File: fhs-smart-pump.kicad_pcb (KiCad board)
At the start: 2 copper layers, 92 x 87 mm, 30 parts, among them J1 Screw_Terminal_01x09, J2 Conn_01x02, J3 Screw_Terminal_01x02, K1 G5NB, K2 G5NB, Q1 2SA1015, Q2 2SA1015, U1 LM2596T-5, U2 PC817, U3 ESP32-C3_SUPERMINI_TH, U4 PC817

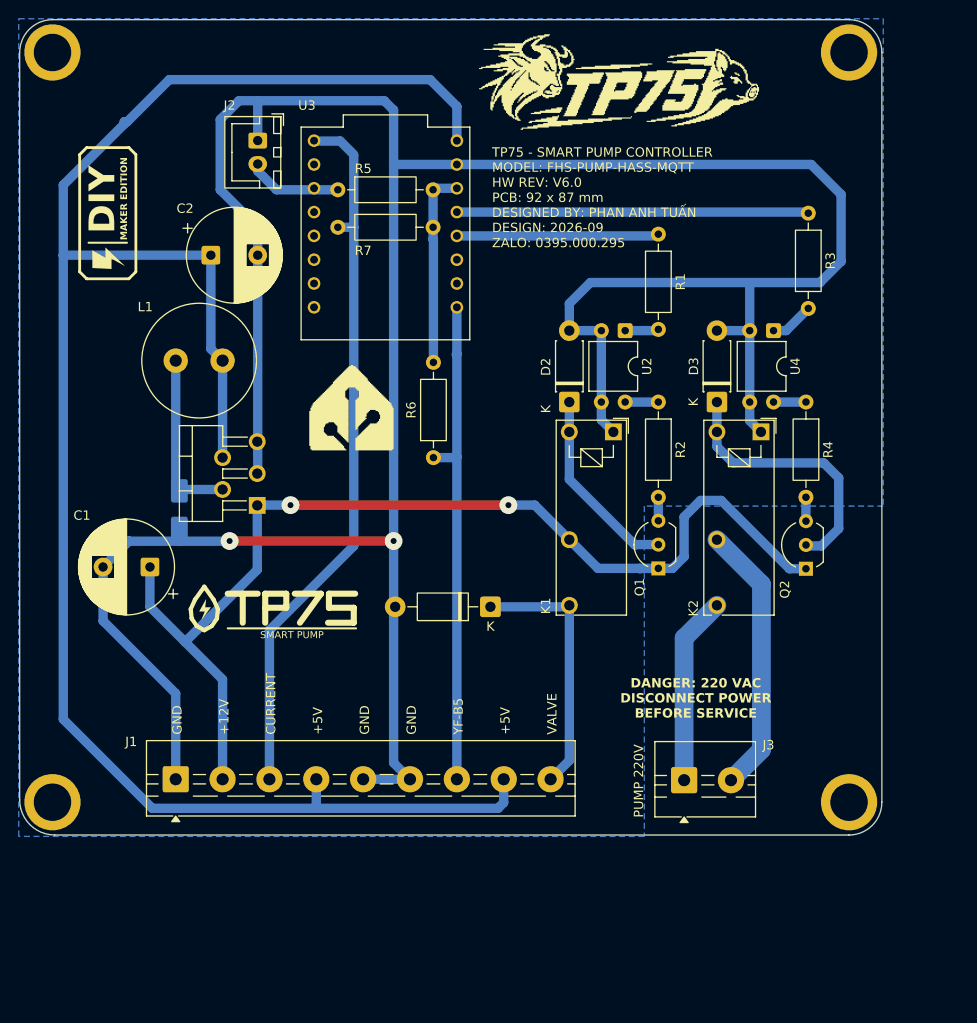
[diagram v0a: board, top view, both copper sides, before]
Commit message: đổi chân nguồn sang 5.5
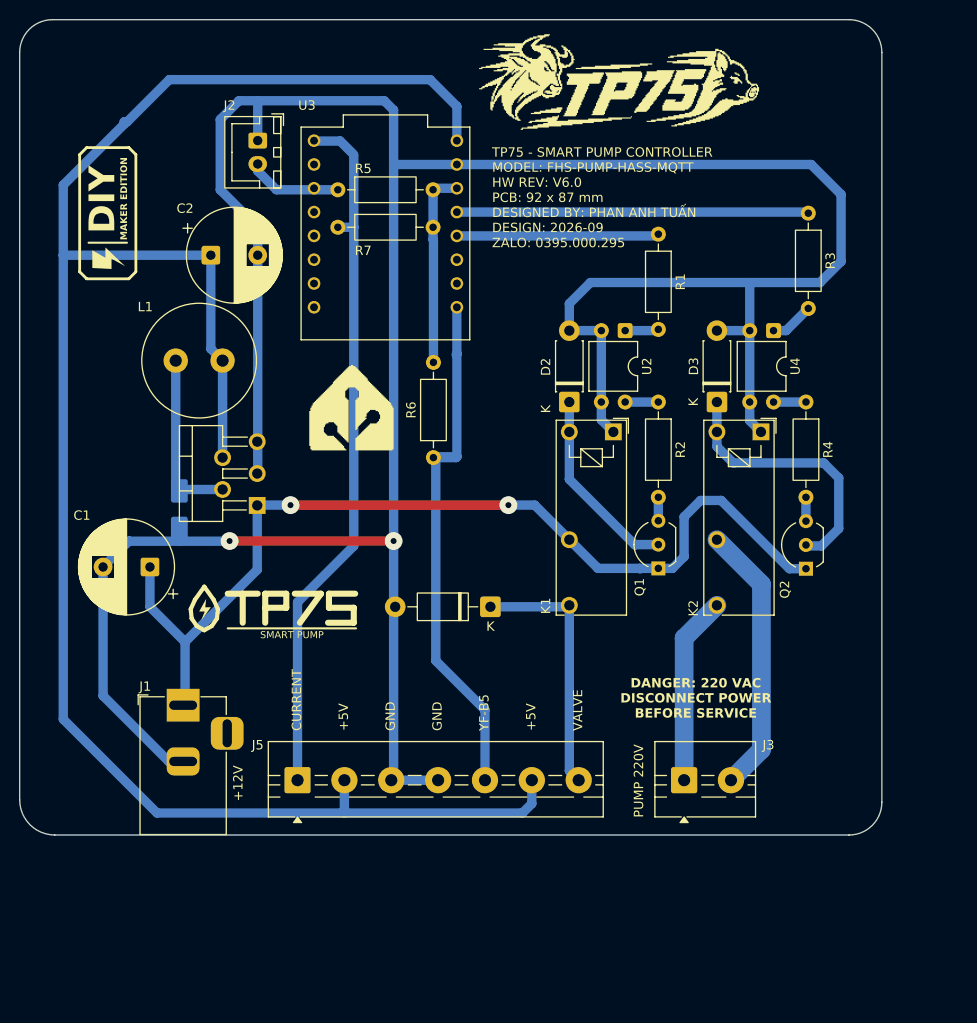
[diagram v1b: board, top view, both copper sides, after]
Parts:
- removed MECH1: LK-PLC02_92x87, 
- added J5: Screw_Terminal_01x07, TerminalBlock:TerminalBlock_MaiXu_MX126-5.0-07P_1x07_P5.00mm, F.Cu at (75.2, 131.0)
- J1: value Screw_Terminal_01x09 -> Barrel_Jack_Switch; footprint TerminalBlock:TerminalBlock_MaiXu_MX126-5.0-09P_1x09_P5.00mm -> Connector_BarrelJack:BarrelJack_Horizontal
- moved J1 7.94 mm to (63.0, 123.0), turned to 90 degrees
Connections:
- J1 pad 1: GND -> +12V
- J1 pad 2: +12V -> GND
- J1 pad 3: /sign-dong-dien -> unconnected-(J1-Pad3)
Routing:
- net +12V: track 113.6 -> 104.1 mm
- net /sign-dong-chay: track 53.0 -> 57.5 mm
- net +5V: track 203.3 -> 207.1 mm
- net GND: track 324.7 -> 323.5 mm
- net /sign-dong-dien: track 76.8 -> 75.7 mm
- removed copper zone on B.Cu, net GND

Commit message: cập nhật bố cục pcb và bổ sung thư viện linh kiện
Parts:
- removed the ? at (81.0, 91.2)
- removed the ? at (73.5, 112.8)
- removed the ? at (55.0, 70.5)
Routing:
- net Net-(D3-K): track 28.9 -> 19.8 mm
- added copper zone on B.Cu, net GND

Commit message: cập nhật cơ khí pcb và báo cáo kiểm tra drc
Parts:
- added MECH1: LK-PLC02_92x87, , F.Cu at (53.8, 150.0)
- moved ? 15.3 mm to (118.0, 69.2)
- moved C1 15.3 mm to (68.0, 121.0)
- moved C2 15.3 mm to (74.5, 87.7)
- moved D1 15.3 mm to (71.1, 114.9)
- moved D2 15.3 mm to (112.8, 103.4)
- moved D3 15.3 mm to (128.5, 103.4)
- moved D4 15.3 mm to (104.3, 125.2)
- moved J2 15.3 mm to (79.5, 75.5)
- moved J3 15.3 mm to (125.0, 143.8)
- moved J5 15.3 mm to (83.8, 143.8)
- moved K1 15.3 mm to (117.5, 106.6)
- moved L1 15.3 mm to (70.8, 99.0)
- moved Q1 15.3 mm to (122.2, 121.2)
- moved Q2 15.3 mm to (138.0, 121.2)
- moved R1 15.3 mm to (122.2, 85.5)
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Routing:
- net +12V: track 104.1 -> 103.5 mm
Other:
- outline, holes or cut-outs redrawn
- board text added: "TP75 - SMART PUMP CONTROLLER MODEL: FHS-PUMP-HASS-MQTT HW REV: V6.0 PCB: 92 x 87 mm DESIGNED BY: PHAN ANH TUAN DESIGN: 2026-09 ZALO: 0395.000.295"
- board text removed: "TP75 - SMART PUMP CONTROLLER MODEL: FHS-PUMP-HASS-MQTT HW REV: V6.0 PCB: 92 x 87 mm DESIGNED BY: PHAN ANH TUẤN DESIGN: 2026-09 ZALO: 0395.000.295"
